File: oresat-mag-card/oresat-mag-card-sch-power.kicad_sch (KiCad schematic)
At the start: 89 parts, among them Q1 DMP2240UDM, Q2 PMV45EN, Q3 DMP3050LVT-7, Q4 DMP3050LVT-7, Q5 PMV45EN, U1 MAX7310, U2 MIC842LYC5, U3 MIC842LYC5, U4 TS5A21366DCUR, U5 MAX4211FETE, U6 TPS62111RSA

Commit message: Moved to independent MT connectors using pico EZ connectors, and re-laid out the STSPIN250s to be more best-practices.
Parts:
- removed TP10, TP12, TP13, TP16, TP18, TP7, TP8, TP9: Test-Point, oresat-misc:TestPoint-0.75mm-th, symbol oresat-misc:Test-Point-0.75mm-th
- C10: DIST (none) -> DigiKey; DPN (none) -> 399-12983-1-ND; MFR (none) -> KEMET; MPN (none) -> C0603C103J5RACAUTO
- C11: DIST (none) -> DigiKey; DPN (none) -> 399-C0603C474K3RACAUTOCT-ND; MFR (none) -> KEMET; MPN (none) -> C0603C474K3RACAUTO
- C2, C3, C5, C7, C9: DIST (none) -> DigiKey; DPN (none) -> 490-GRT188R71E105KE13DCT-ND; MFR (none) -> Murata Electronics; MPN (none) -> GRT188R71E105KE13D
- C4, C6, C71, C72: DIST (none) -> DigiKey; DPN (none) -> 399-6856-1-ND; MFR (none) -> KEMET; MPN (none) -> C0603C104K5RACAUTO
- C8: DIST (none) -> DigiKey; DPN (none) -> 490-GRT21BC71E106KE13KCT-ND; MFR (none) -> Murata Electronics; MPN (none) -> GRT21BC71E106KE13K
- D1: DIST (none) -> DigiKey; DPN (none) -> 732-150060AS75000CT-ND; MFR (none) -> Wurth; MPN (none) -> 150060AS75000
- D2, D3: DIST (none) -> DigiKey; DPN (none) -> 732-4971-1-ND; MFR (none) -> Wurth; MPN (none) -> 150060GS75000
- L1: DIST (none) -> DigiKey; DPN (none) -> XC2337CT-ND; MFR (none) -> ECS; MPN (none) -> ECS-MPI4040R4-6R8-R
- Q1: value DMP2240UDM -> DMP2240UDM-7; DIST (none) -> DigiKey; MPN DMP2240UDM -> DMP2240UDM-7
- Q2, Q5: value PMV45EN -> DMN3028LQ-7; DIST (none) -> DigiKey; DPN 1727-2307-1-ND -> 31-DMN3028LQ-7CT-ND; MFR Nexperia -> Diodes Incorporated; MPN PMV45EN2R -> DMN3028LQ-7
- Q3, Q4: value DMP3050LVT-7 -> DMPH2040UVTQ-7; DIST (none) -> DigiKey; DPN DMP3050LVT-7DICT-ND -> 31-DMPH2040UVTQ-7CT-ND; MFR Diodes Inc -> Diodes Incorporated; MPN DMP3050LVT-7 -> DMPH2040UVTQ-7
- R1: DIST (none) -> DigiKey; DPN (none) -> RMCF0603FT10R0CT-ND; MFR (none) -> Stackpole Electronics; MPN (none) -> RMCF0603FT10R0
- R10, R11, R12, R13, R16, R17, R2, R27, R28, R3, R4, R5, R6, R7, R8, R9: DIST (none) -> DigiKey; DPN (none) -> RMCF0603FT100RCT-ND; MFR (none) -> Stackpole Electronics; MPN (none) -> RMCF0603FT100R
- R14, R15: DIST (none) -> DigiKey; DPN (none) -> RMCF0603FT665KCT-ND; MFR (none) -> Stackpole Electronics; MPN (none) -> RMCF0603FT665K
- R18, R23, R24, R26, R30, R32, R34, R39, R40, R41, R42, R43, R44: DIST (none) -> DigiKey; DPN (none) -> RMCF0603FT10K0CT-ND; MFR (none) -> Stackpole Electronics; MPN (none) -> RMCF0603FT10K0
- R19, R20: DIST (none) -> DigiKey; DPN (none) -> RMCF0603FT330KCT-ND; MFR (none) -> Stackpole Electronics; MPN (none) -> RMCF0603FT330K
- R21, R22: DIST (none) -> DigiKey; DPN (none) -> RMCF0603FT1M00CT-ND; MFR (none) -> Stackpole Electronics; MPN (none) -> RMCF0603FT1M00
- R25: DIST (none) -> DigiKey; DPN (none) -> RMCF0603FT4K70CT-ND; MFR (none) -> Stackpole Electronics; MPN (none) -> RMCF0603FT4K70
- R29: DIST (none) -> DigiKey; DPN (none) -> RMCF0603FT100KCT-ND; MFR (none) -> Stackpole Electronics; MPN (none) -> RMCF0603FT100K
- R31: DIST (none) -> DigiKey; DPN (none) -> 738-CSS0805FT15L0CT-ND; MFR (none) -> Stackpole Electronics; MPN (none) -> CSS0805FT15L0
- R35, R36, R37, R38: DIST (none) -> DigiKey; DPN (none) -> RMCF0603ZT0R00CT-ND; MFR (none) -> Stackpole Electronics; MPN (none) -> RMCF0603ZT0R00
- U1: DIST (none) -> DigiKey; MFR Maxim -> Analog Devices; MPN MAX7310ATE -> MAX7310ATE+
- U2, U3: DIST (none) -> DigiKey; DPN (none) -> 576-2927-1-ND; MFR (none) -> Microchip; MPN (none) -> MIC842LYC5-TR
- U4, U5, U6: DIST (none) -> DigiKey
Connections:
- no-connect marks 2 -> 3
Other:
- note added: "Main Power Switch Vbus = (6.0,7.2,8.4)V"
- note removed: "Main Power Switch"
- note removed: "Vbus = (6.0,7.2,8.4)V"
- moved on the sheet: C10, C11, C12, C2, C3, C4, C5, C6, C7, C71, C72, C8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

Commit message: Final mag card
Lots of polishing around best practices layout. Put in giant hole to thread the MTs from below if required for the 3U CubeSats. Cleaned up power layer, added stitching vias, updated readme.
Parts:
- C10, C11, C2, C3, C4, C5, C6, C7, C71, C72, C9, D1, D2, D3, L1, R1, R14, R15, R17, R18, R19, R20, R21, R22, R23, R24, R25, R26, R27, R28, R29, R30, R31, R32, R34, R35, R36, R39, R40, R41, R42, R43, R44, R5, R6, R7, R9, U2, U3: DIS (none) -> DigiKey; DIST DigiKey -> (none)
- C12: DIS (none) -> DigiKey
- C8: DIS (none) -> DigiKey; DIST DigiKey -> (none); Size 0805 -> (none)
- Q1, Q2, Q3, Q4, Q5, U1, U5, U6: DIS Digi-Key -> DigiKey; DIST DigiKey -> (none)
- R10, R11, R12, R13, R16, R2, R3, R37, R38, R4, R8, U4: DIST DigiKey -> (none)

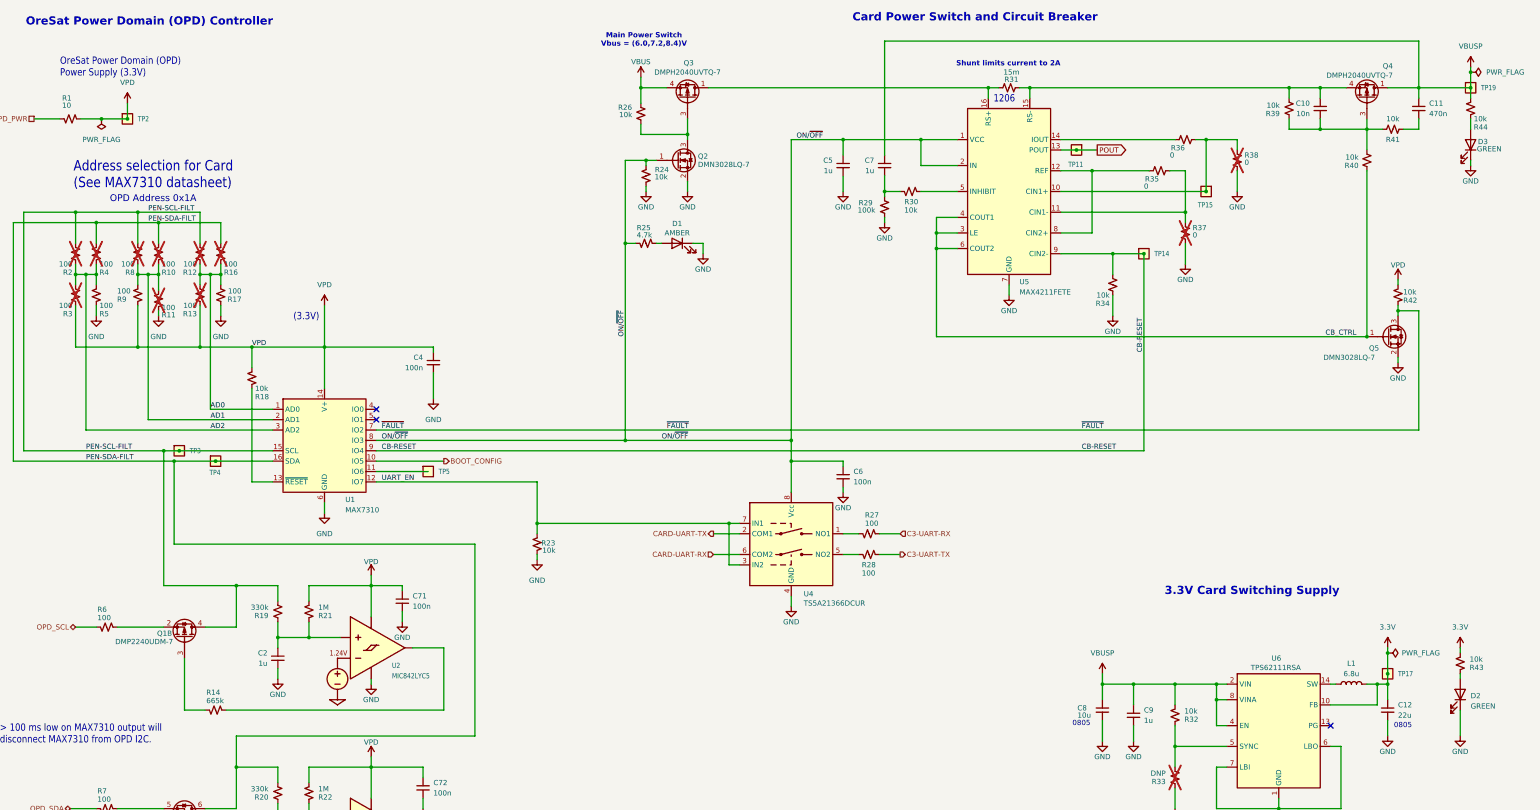
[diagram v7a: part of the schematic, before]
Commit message: Upgraded to kiCad 10, updated BOM during fabrication woes with Colorodo PCBA, no change in PCB
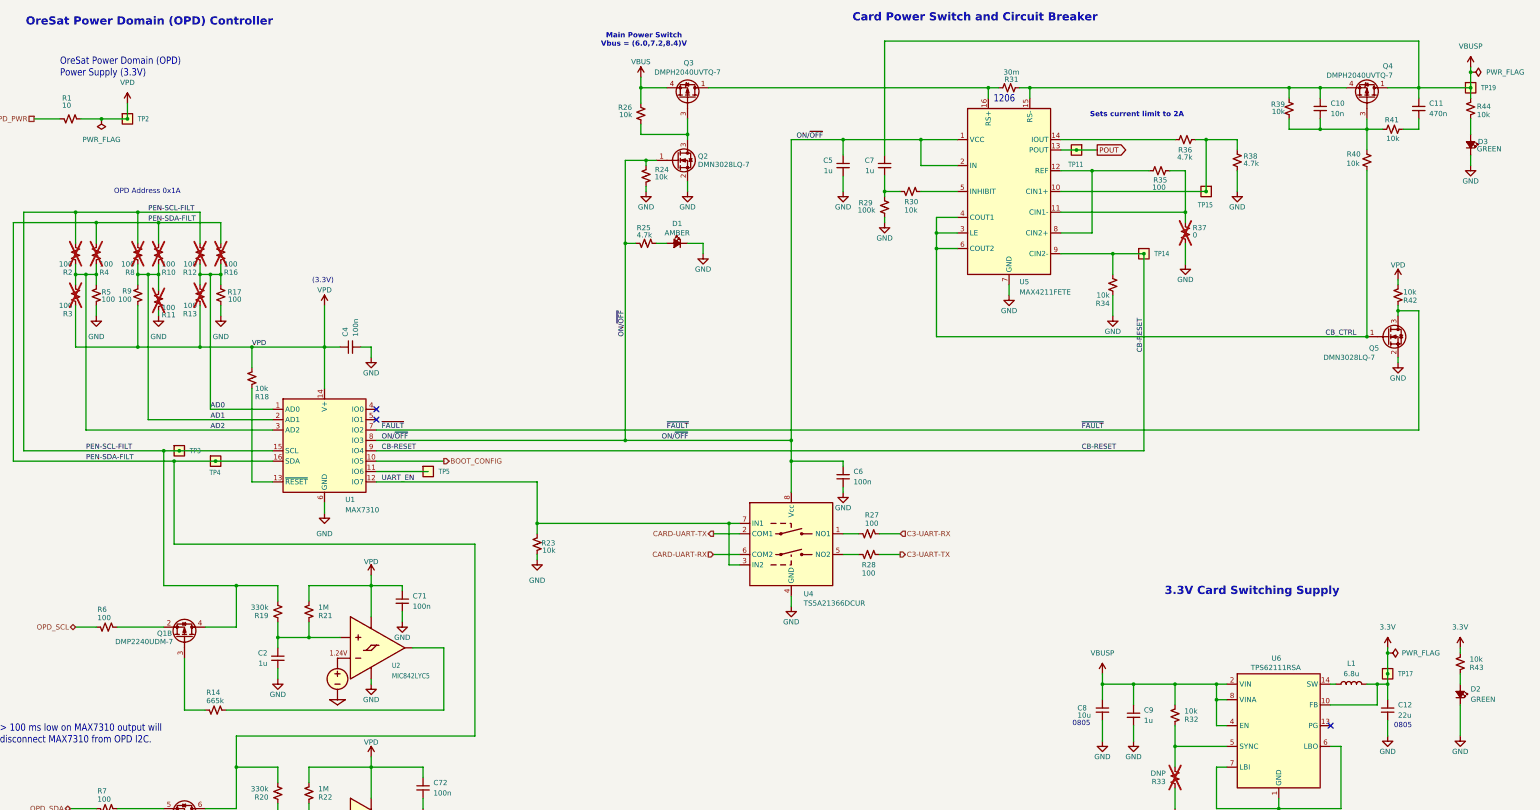
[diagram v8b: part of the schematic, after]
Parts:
- C10, C11, C2, C3, C4, C5, C6, C7, C71, C72, C8, C9, L1, Q1, Q2, Q3, Q4, Q5, R1, R14, R15, R17, R18, R19, R20, R21, R22, R23, R24, R25, R26, R27, R28, R29, R30, R32, R34, R39, R40, R41, R42, R43, R44, R5, R6, R7, R9, U1, U2, U3, U4, U5, U6: DIST (none) -> DigiKey
- C12: DIST (none) -> DigiKey; DPN (none) -> 490-GRT21BC81C226ME13LCT-ND; MFR (none) -> Murata Electronics; MPN (none) -> GRT21BC81C226ME13L
- D1, D2, D3: symbol Device:LED -> Device:LED_Small_Filled; DIST (none) -> DigiKey
- R31: value 15m -> 30m; DIST (none) -> DigiKey; DPN 738-CSS0805FT15L0CT-ND -> CSR1206FK30L0CT-ND; MPN CSS0805FT15L0 -> CSR1206FK30L0
- R35: value 0 -> 100; DIST (none) -> DigiKey; DPN RMCF0603ZT0R00CT-ND -> RMCF0603FT100RCT-ND; MPN RMCF0603ZT0R00 -> RMCF0603FT100R
- R36: value 0 -> 4.7k; DIST (none) -> DigiKey; DPN RMCF0603ZT0R00CT-ND -> RMCF0603FT4K70CT-ND; MPN RMCF0603ZT0R00 -> RMCF0603FT4K70
- R38: value 0 -> 4.7k; DIST (none) -> DigiKey; DPN RMCF0603ZT0R00CT-ND -> RMCF0603FT4K70CT-ND; MPN RMCF0603ZT0R00 -> RMCF0603FT4K70; now fitted
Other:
- note added: "Sets current limit to 2A"
- note removed: "Address selection for Card (See MAX7310 datasheet)"
- note removed: "Shunt limits current to 2A"
- moved on the sheet: C4
